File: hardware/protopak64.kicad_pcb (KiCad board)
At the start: 2 copper layers, 47.8 x 108.7 mm, 4 parts, among them J1 PakEdge, J2 Breakout2x16

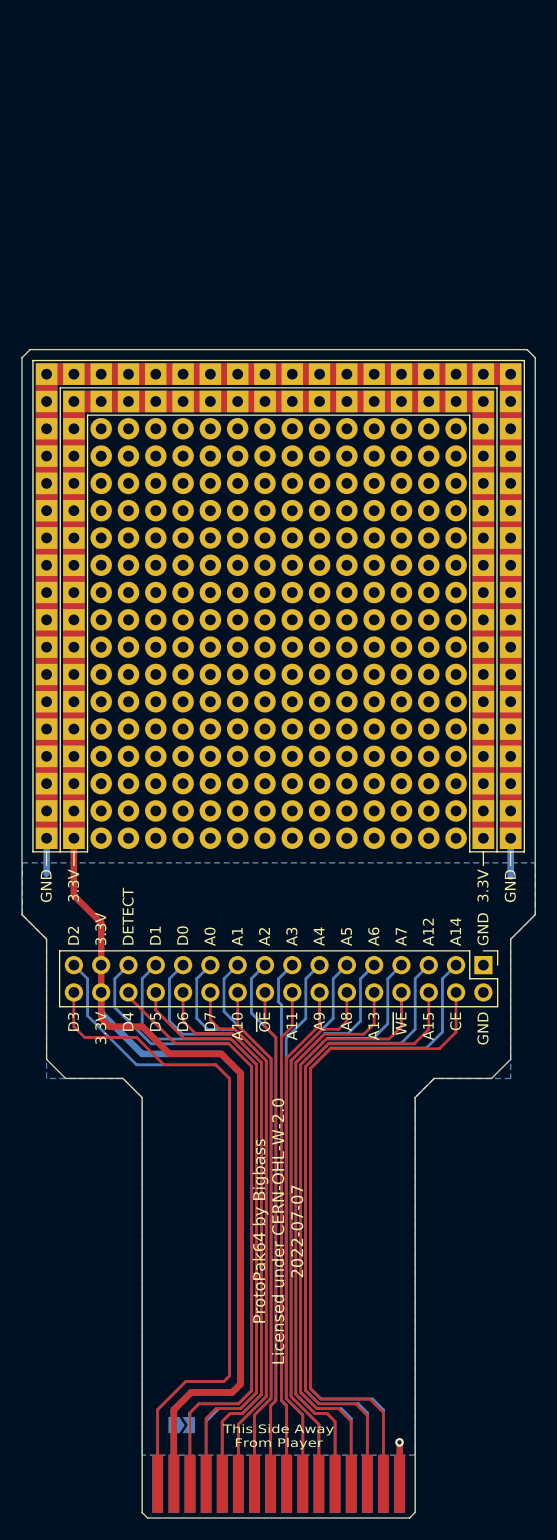
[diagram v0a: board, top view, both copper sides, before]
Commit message: Extended hole grid, added second set of headers, and adjusted orientation details.
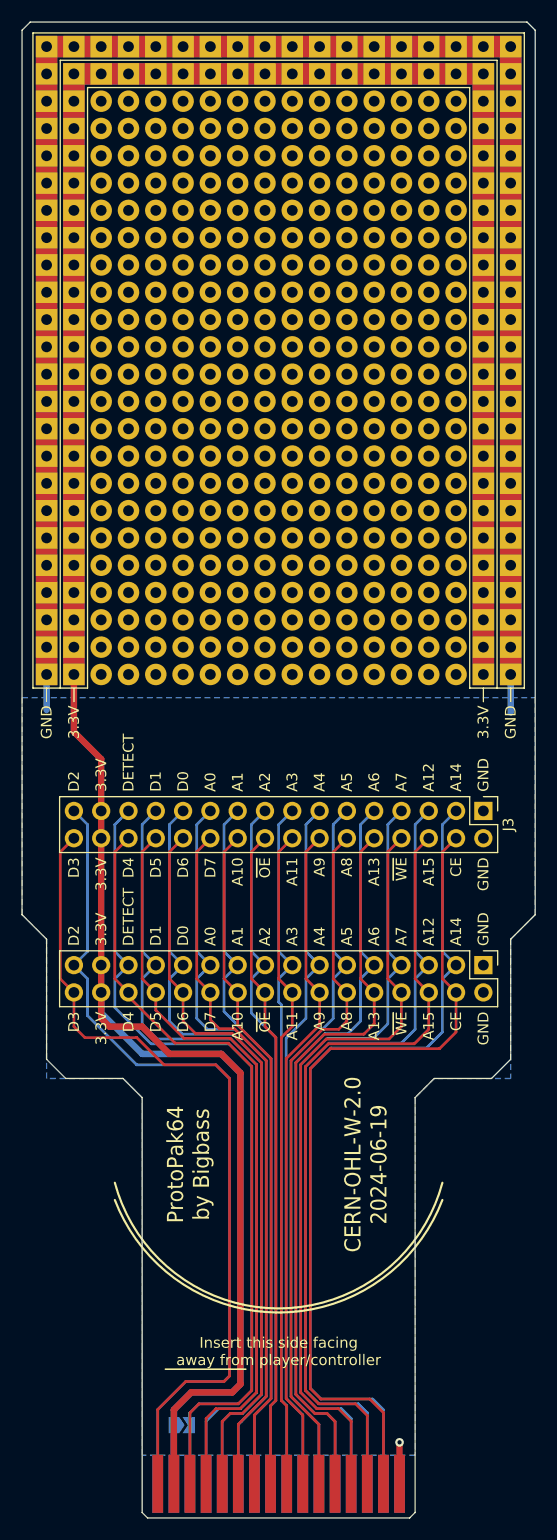
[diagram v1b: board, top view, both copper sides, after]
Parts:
- added J3: Breakout2x16, Connector_PinHeader_2.54mm:PinHeader_2x16_P2.54mm_Vertical, F.Cu at (162.8, 89.4)
- moved REF** 3.81 mm to (143.8, 76.7)
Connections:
- REF** pad 307: GND -> (no net)
- REF** pad 308: +3V3 -> (no net)
- REF** pad 324: GND -> (no net)
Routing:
- net A14: track 64.7 -> 80.1 mm
- net DETECT: track 62.9 -> 78.3 mm
- net D5: track 55.4 -> 70.8 mm
- net CE: track 62.8 -> 78.2 mm
- net A2: track 49.9 -> 65.3 mm
- net D4: track 57.9 -> 73.3 mm
- net A9: track 47.7 -> 63.1 mm
- net A6: track 54.7 -> 70.1 mm
- net A5: track 51.5 -> 66.9 mm
- net A4: track 50.2 -> 65.6 mm
- net A15: track 59.6 -> 74.9 mm
- net A13: track 53.1 -> 68.5 mm
- net A10: track 47.7 -> 63.1 mm
- net A1: track 51.2 -> 66.6 mm
- net ~{OE}: track 46.4 -> 61.7 mm
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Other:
- board size 47.8 x 108.7 mm -> 47.8 x 139.2 mm
- board text added: "CERN-OHL-W-2.0 2024-06-19"
- board text added: "Insert this side facing away from player/controller"
- board text added: "Insert with this side facing toward player/controller"
- board text added: "ProtoPak64 by Bigbass"
- board text removed: "ProtoPak64 by Bigbass Licensed under CERN-OHL-W-2.0 2022-07-07"
- board text removed: "This Side Away From Player"
- board text removed: "This Side Toward Player"
